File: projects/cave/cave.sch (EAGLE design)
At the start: 111 parts, among them U1 IRLML6344TRPBF, U10 IRLML6344TRPBF, U11 IRLML6344TRPBF, U12 IRLML6344TRPBF, U2 TLC555CDR, U3 IRLML6344TRPBF, U4 IRLML6344TRPBF, U5 IRLML6344TRPBF, U6 IRLML6344TRPBF, U7 TPS54625, U9 IRLML6344TRPBF

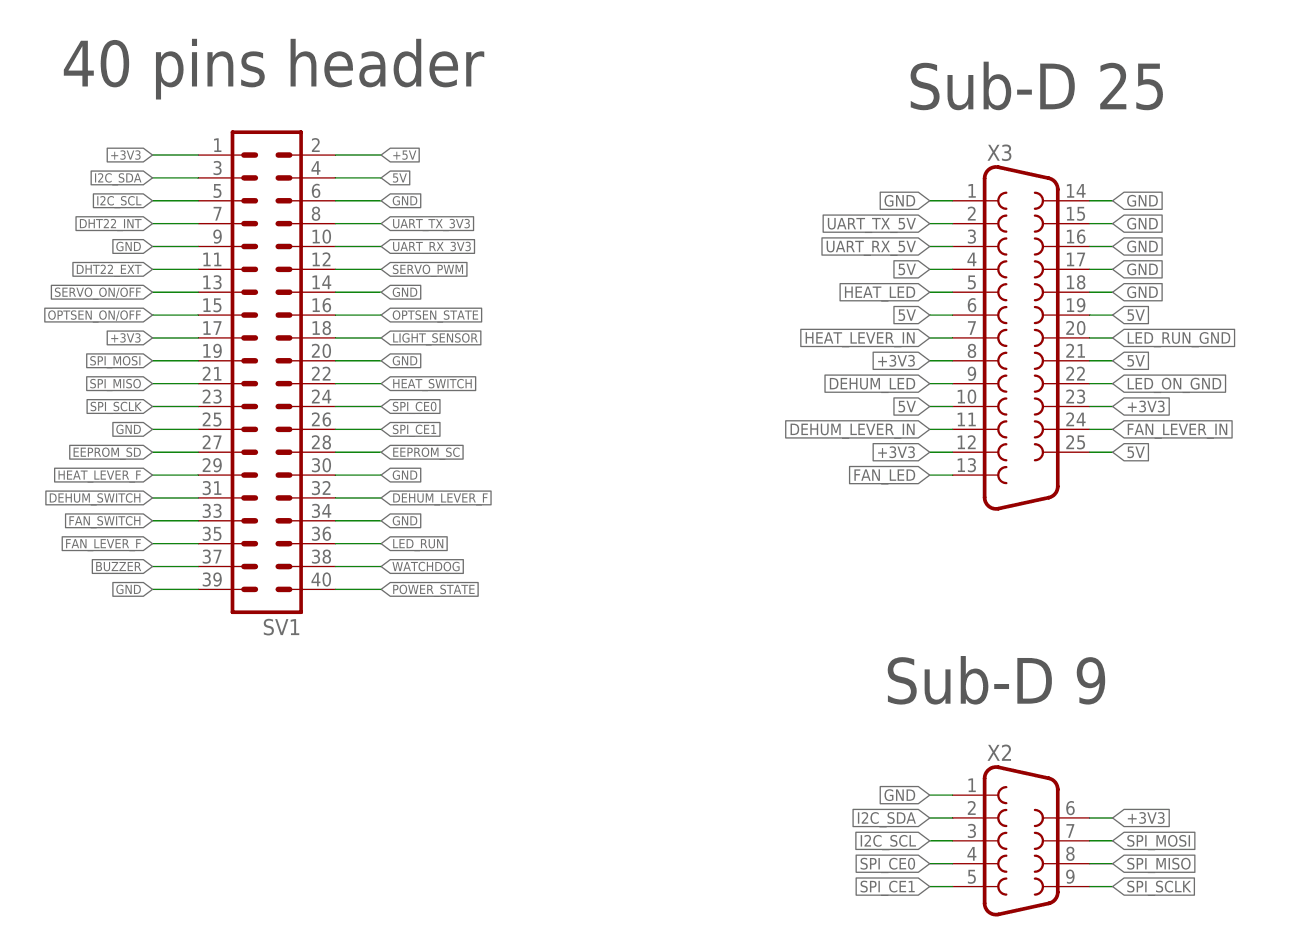
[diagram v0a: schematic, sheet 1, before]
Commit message: Routing done !! Changed 5V to +5V on 25-pin Sub-D. Modified Routing_prefs script.
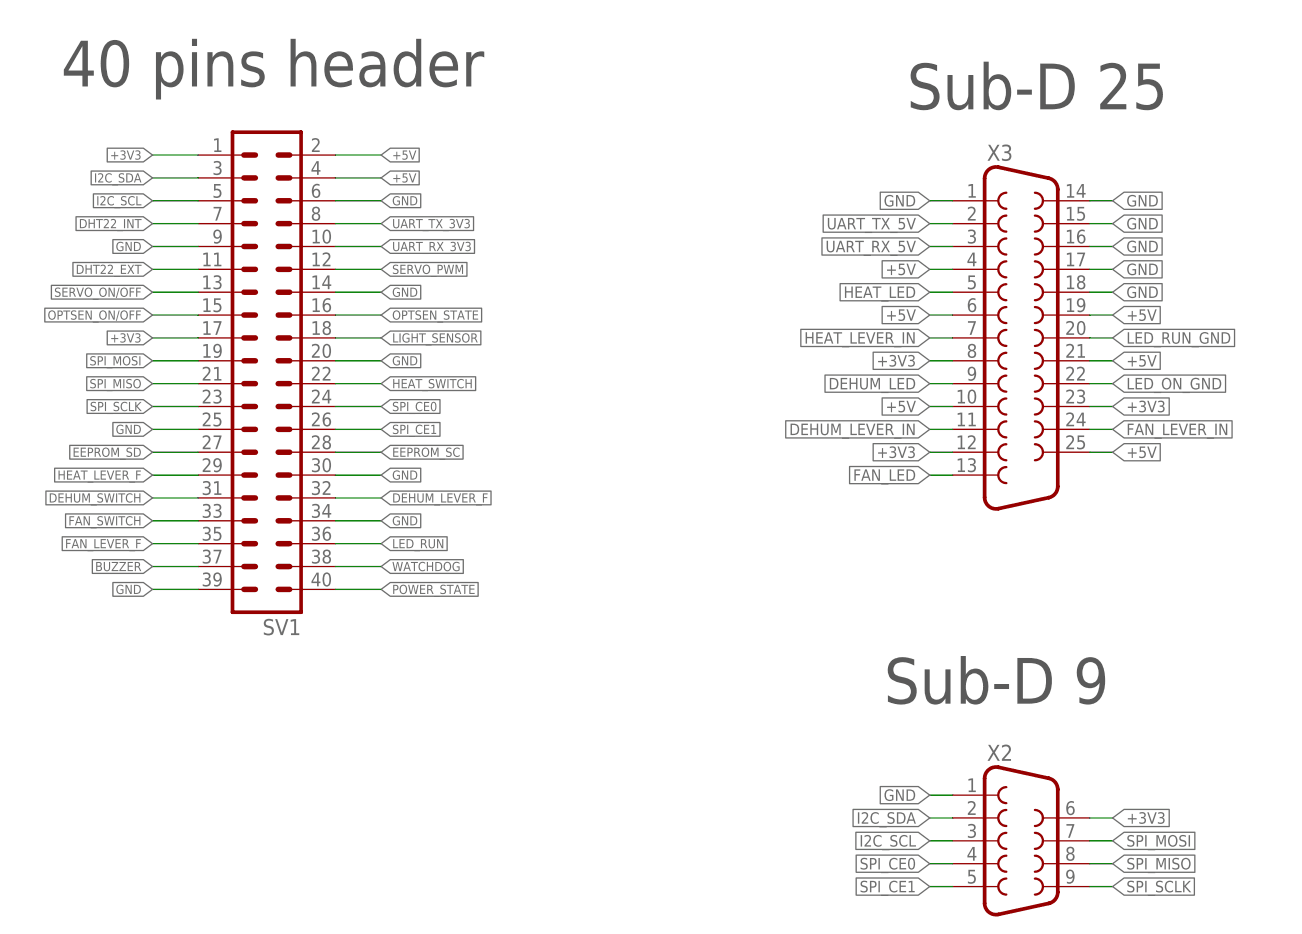
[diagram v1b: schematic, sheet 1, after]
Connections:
- removed net 5V: SV1.4, X3.10, X3.19, X3.21, X3.25, X3.4, X3.6
- net +5V: now also SV1.4, X3.10, X3.19, X3.21, X3.25, X3.4, X3.6

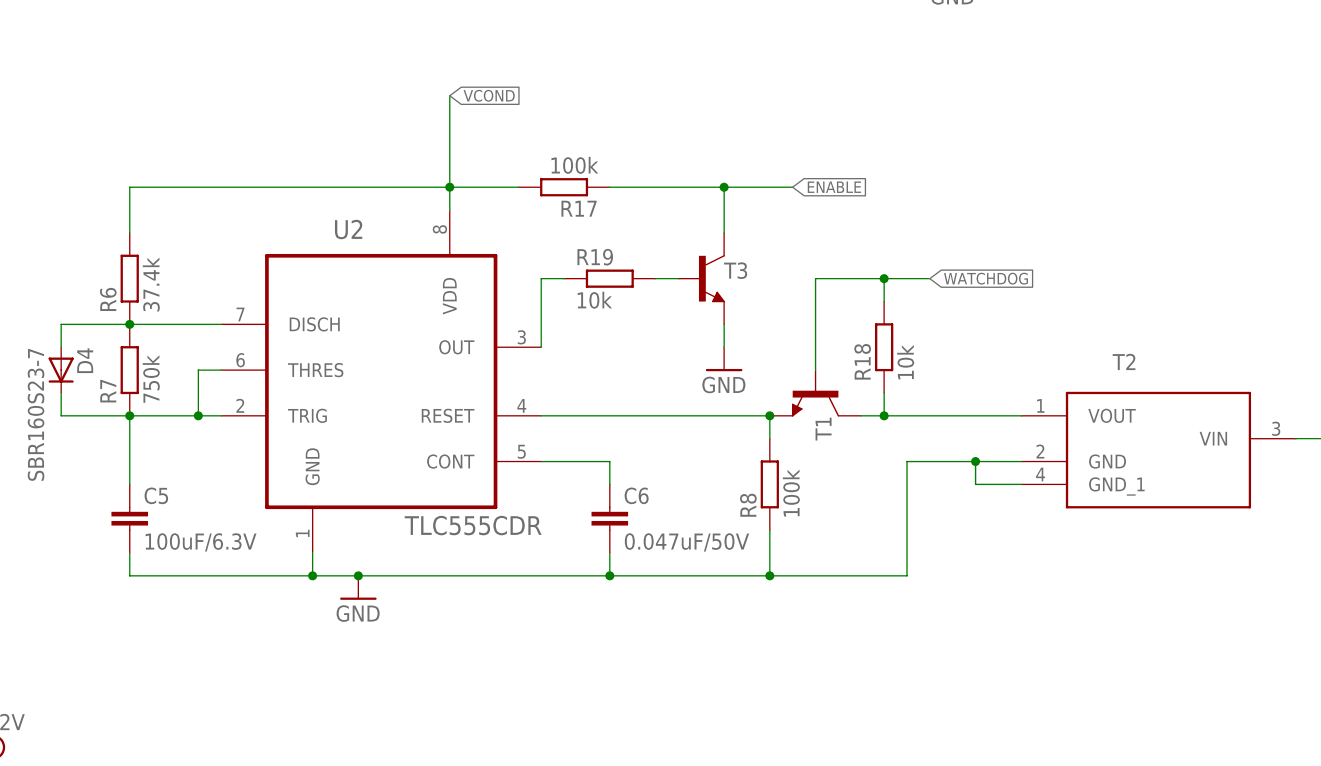
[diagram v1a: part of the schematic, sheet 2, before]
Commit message: Added silkscreen on board (_tsilk layer). Changed GND pin name in STM library (moved to personnal lib).
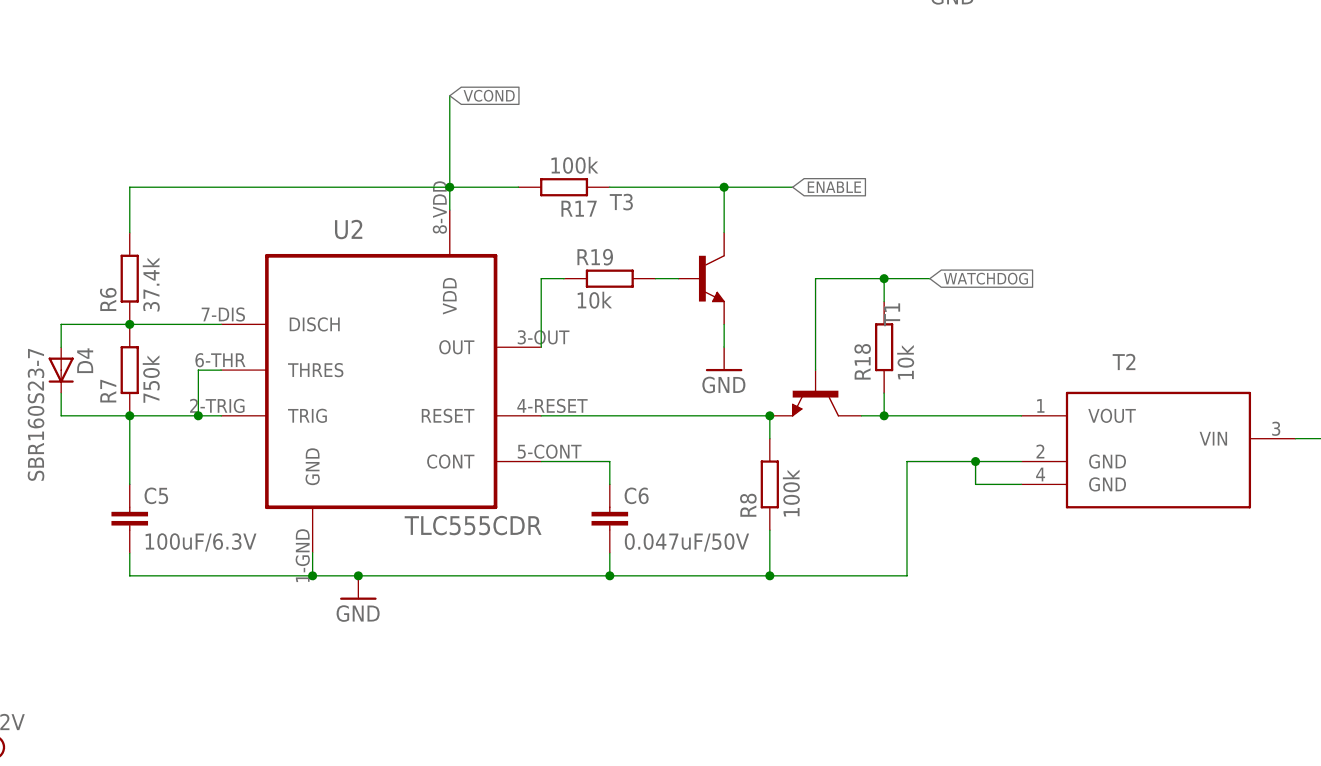
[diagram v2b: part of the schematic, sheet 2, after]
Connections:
- net GND: now also T2.GND@1, T2.GND@2; no longer T2.GND, T2.GND_1
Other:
- moved on the sheet: U2
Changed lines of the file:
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@@
 <wire x1="139.7" y1="-25.4" x2="121.92" y2="-25.4" width="0.1524" layer="91"/>
 <junction x="121.92" y="-25.4"/>
-<pinref part="T2" gate="A" pin="GND"/>
+<pinref part="T2" gate="A" pin="GND@1"/>
 <wire x1="167.64" y1="-12.7" x2="162.56" y2="-12.7" width="0.1524" layer="91"/>
 <wire x1="162.56" y1="-12.7" x2="154.94" y2="-12.7" width="0.1524" layer="91"/>
@@
 <wire x1="154.94" y1="-25.4" x2="139.7" y2="-25.4" width="0.1524" layer="91"/>
 <junction x="139.7" y="-25.4"/>
-<pinref part="T2" gate="A" pin="GND_1"/>
+<pinref part="T2" gate="A" pin="GND@2"/>
 <wire x1="167.64" y1="-15.24" x2="162.56" y2="-15.24" width="0.1524" layer="91"/>
 <wire x1="162.56" y1="-15.24" x2="162.56" y2="-12.7" width="0.1524" layer="91"/>

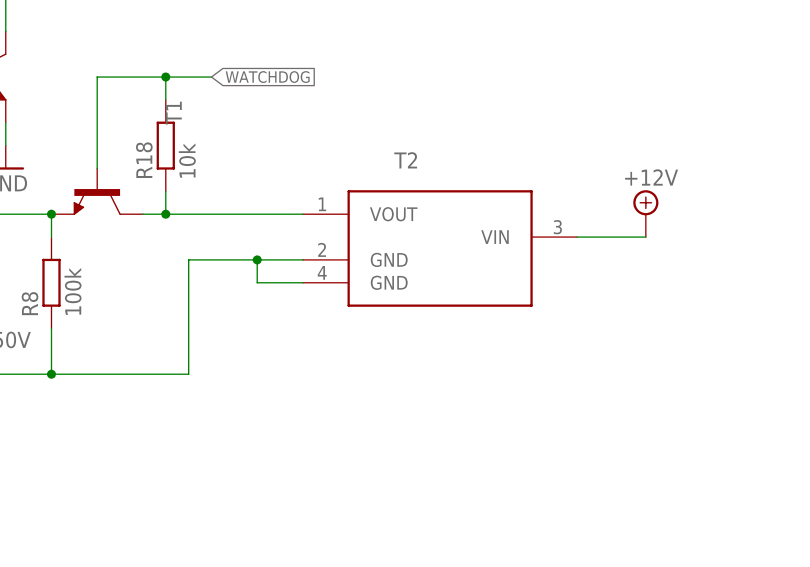
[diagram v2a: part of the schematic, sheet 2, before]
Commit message: Silkscreen moved to tDocu layer. Added some space between the MOSFET. Modified 40-pin-header package's silkscreen and saved it to HE_254.lbr.
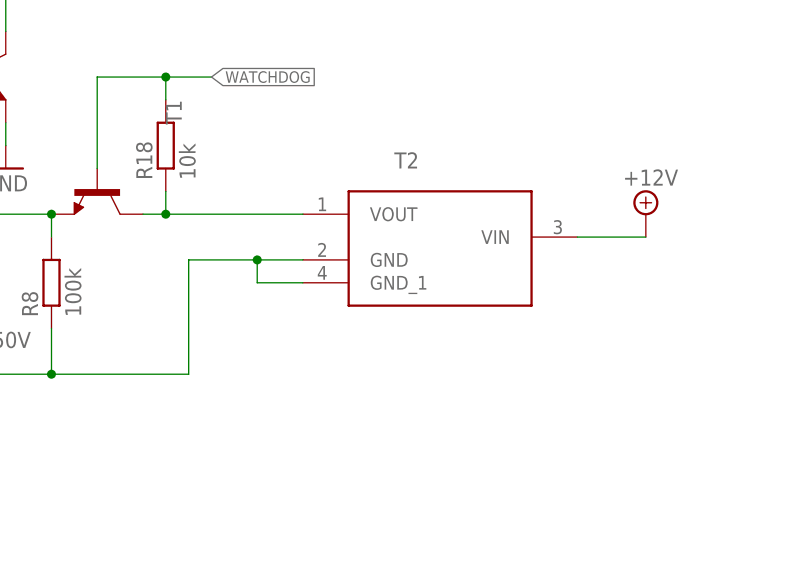
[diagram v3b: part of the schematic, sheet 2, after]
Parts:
- SV1: device con-lstb:MA20-2 -> HE_254:MA20-2
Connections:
- net GND: now also T2.GND, T2.GND_1; no longer T2.GND@1, T2.GND@2
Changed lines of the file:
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@@
 </classes>
 <parts>
-<part name="SV1" library="con-lstb" deviceset="MA20-2" device=""/>
+<part name="SV1" library="HE_254" deviceset="MA20-2" device=""/>
 <part name="D2" library="semicon-smd-ipc" deviceset="D-" device="A1-C3" value="SBR160S23-7"/>
 <part name="D1" library="semicon-smd-ipc" deviceset="D-" device="A1-C3" value="SBR160S23-7"/>
@@
 <wire x1="139.7" y1="-25.4" x2="121.92" y2="-25.4" width="0.1524" layer="91"/>
 <junction x="121.92" y="-25.4"/>
-<pinref part="T2" gate="A" pin="GND@1"/>
+<pinref part="T2" gate="A" pin="GND"/>
 <wire x1="167.64" y1="-12.7" x2="162.56" y2="-12.7" width="0.1524" layer="91"/>
 <wire x1="162.56" y1="-12.7" x2="154.94" y2="-12.7" width="0.1524" layer="91"/>
@@
 <wire x1="154.94" y1="-25.4" x2="139.7" y2="-25.4" width="0.1524" layer="91"/>
 <junction x="139.7" y="-25.4"/>
-<pinref part="T2" gate="A" pin="GND@2"/>
+<pinref part="T2" gate="A" pin="GND_1"/>
 <wire x1="167.64" y1="-15.24" x2="162.56" y2="-15.24" width="0.1524" layer="91"/>
 <wire x1="162.56" y1="-15.24" x2="162.56" y2="-12.7" width="0.1524" layer="91"/>
